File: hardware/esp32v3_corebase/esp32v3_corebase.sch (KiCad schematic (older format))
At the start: 47 parts, among them J1 USB_C_Receptacle_USB2.0, Q1 MBT2222ADW1T1, U1 TLV75533PDBV, U3 W25Q32FVSS, U4 CH340C, U5 ESP32, Y1 40MHz 10ppm

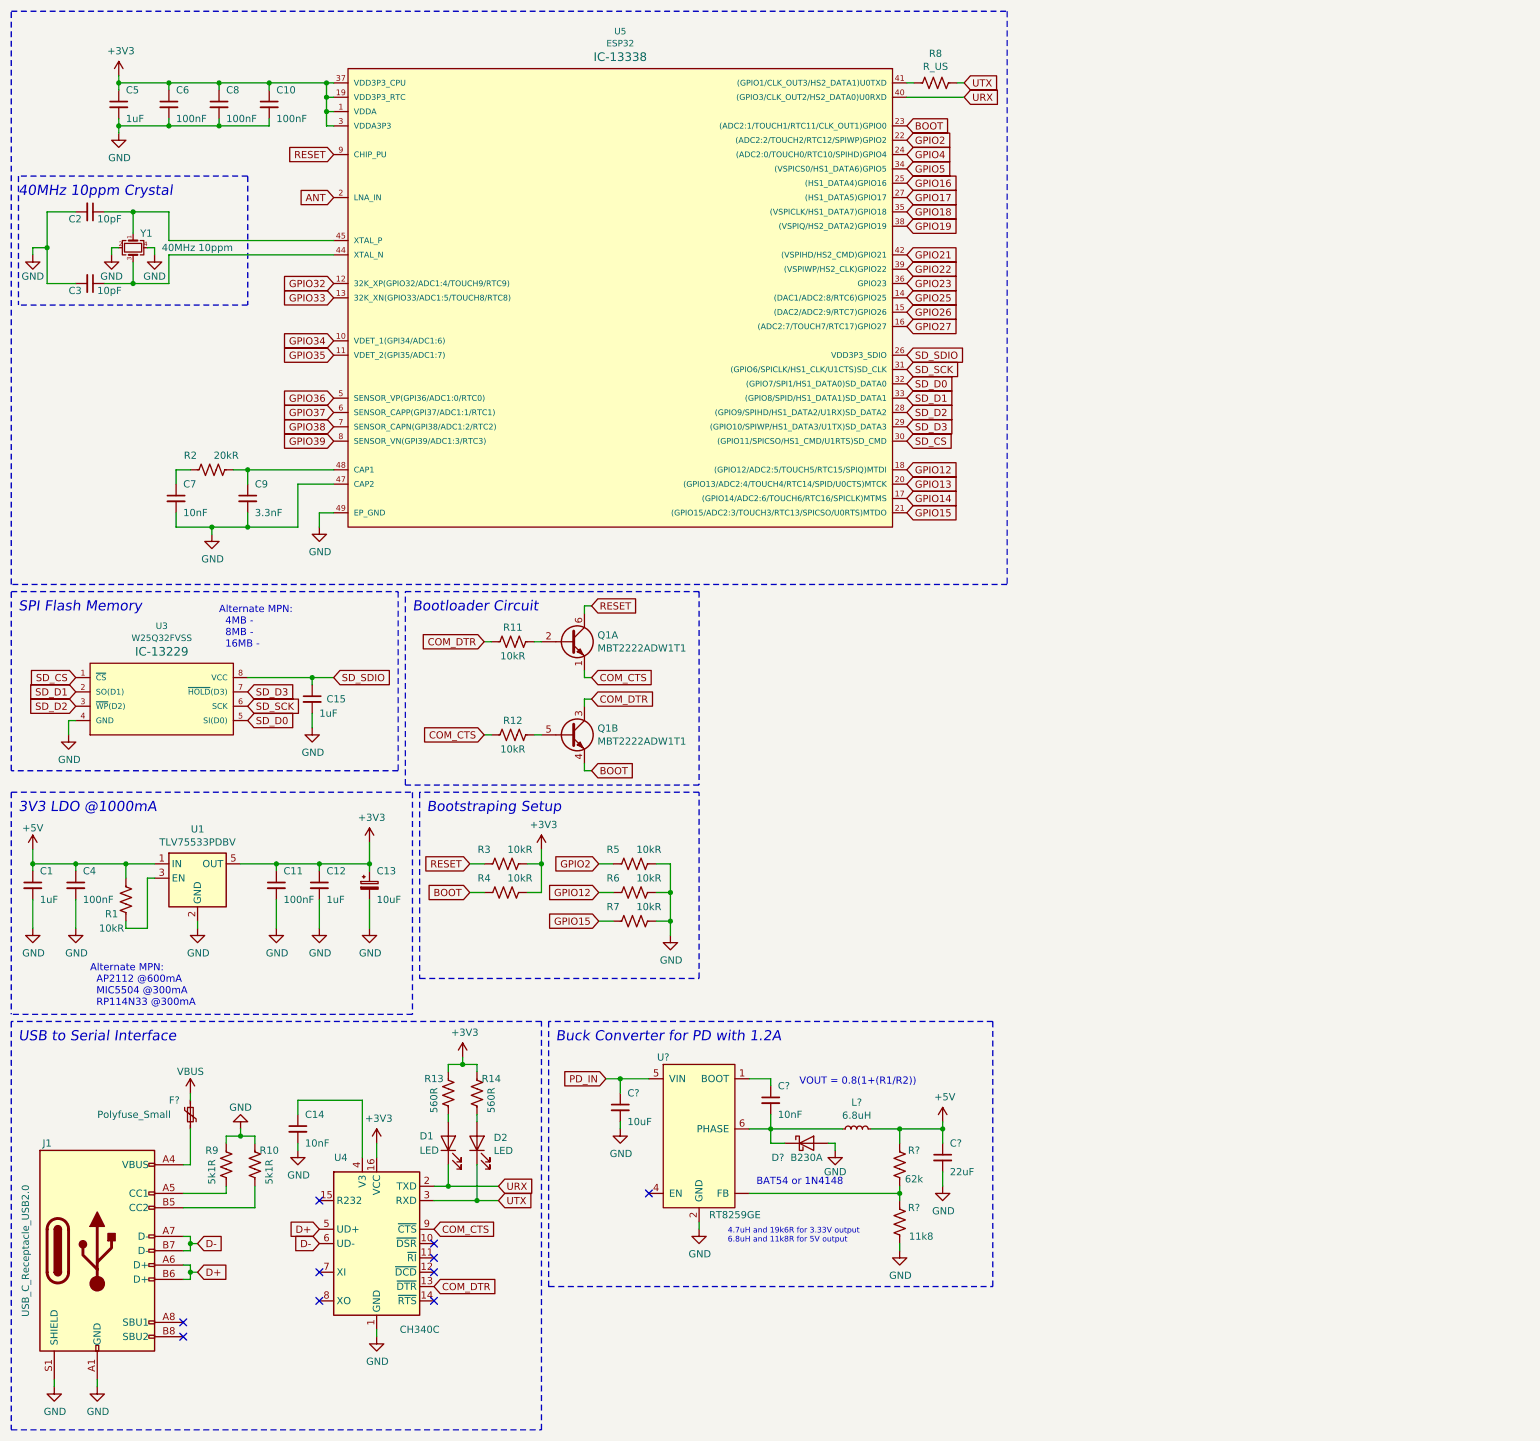
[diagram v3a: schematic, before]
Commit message: Added PSRAM and minor changes on sch
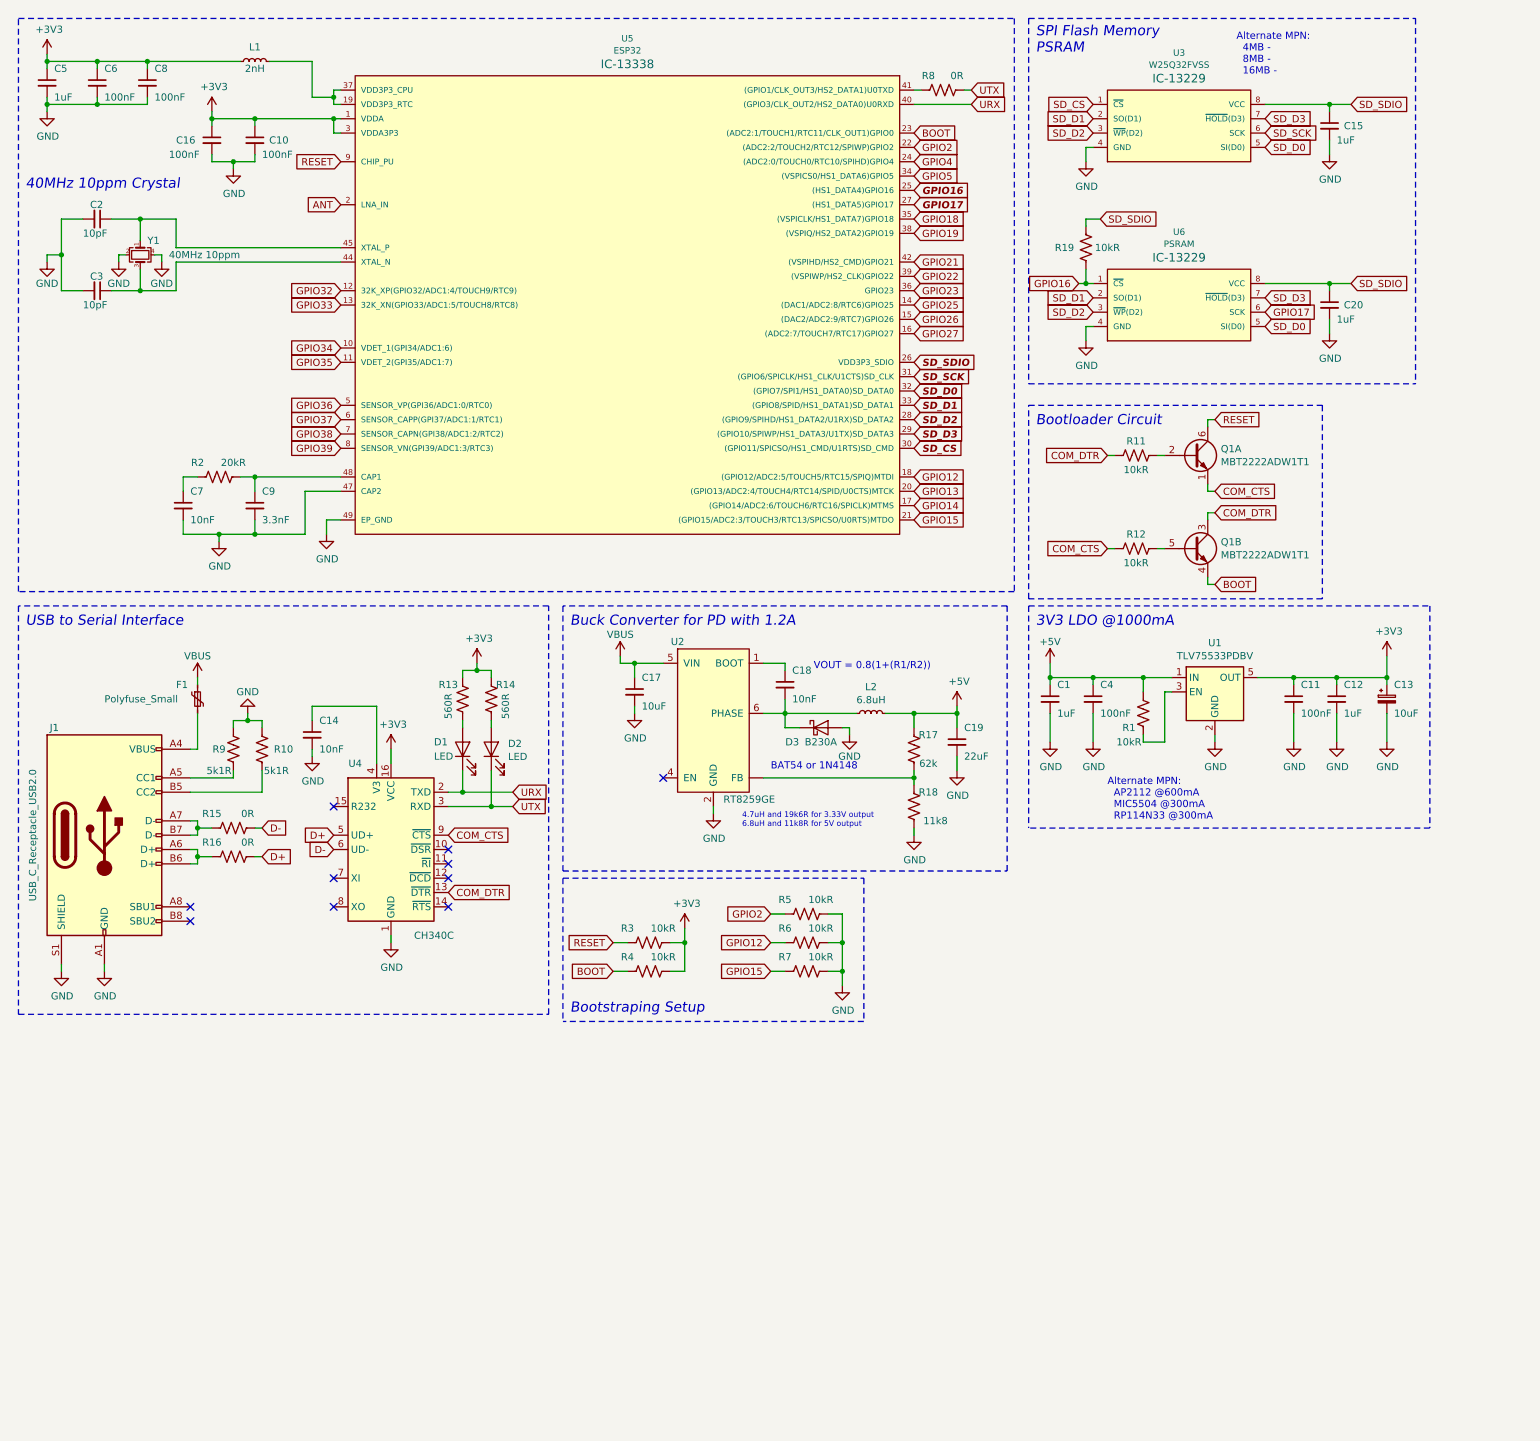
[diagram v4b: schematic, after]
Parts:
- added C16: 100nF, Capacitor_SMD:C_0402_1005Metric, symbol Device:C_Small
- added C20: 1uF, Capacitor_SMD:C_0603_1608Metric, symbol Device:C_Small
- added L1: 2nH, symbol Device:L_Small
- added R15, R16: 0R, Resistor_SMD:R_0402_1005Metric, symbol Device:R_US
- added R19: 10kR, Resistor_SMD:R_0402_1005Metric, symbol Device:R_US
- added U6: PSRAM, Silicon-Standard:SOIC-8, symbol SparkFun-IC-Memory:W25Q32FVSS
- R8: value R_US -> 0R
- gave numbers to parts that had none: 9
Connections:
- net PD_IN is gone; now on net VBUS: C17.1, U2.5 (VIN)
- net +3V3: now also C16.1, L1.1; no longer U5.19 (VDD3P3_RTC), U5.37 (VDD3P3_CPU)
- net D+: now also R16.1; no longer J1.A6 (D+), J1.B6 (D+)
- net D-: now also R15.1; no longer J1.A7 (D-), J1.B7 (D-)
- net GND: now also C16.2, C20.2, U6.4 (GND)
- net GPIO16: now also R19.1, U6.1 (~CS~)
- net GPIO17: now also U6.6 (SCK)
- net SD_D0: now also U6.5 (SI(D0))
- net SD_D1: now also U6.2 (SO(D1))
- net SD_D2: now also U6.3 (~WP~(D2))
- net SD_D3: now also U6.7 (~HOLD~(D3))
- net SD_SDIO: now also C20.1, R19.2, U6.8 (VCC)
- new net: J1.A6 (D+), J1.B6 (D+), R16.2
- new net: J1.A7 (D-), J1.B7 (D-), R15.2
- new net: L1.2, U5.19 (VDD3P3_RTC), U5.37 (VDD3P3_CPU)
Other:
- note added: "SPI Flash Memory\nPSRAM"
- note removed: "SPI Flash Memory"
- moved on the sheet: C1, C10, C11, C12, C13, C14, C15, C17, C18, C19, C2, C3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

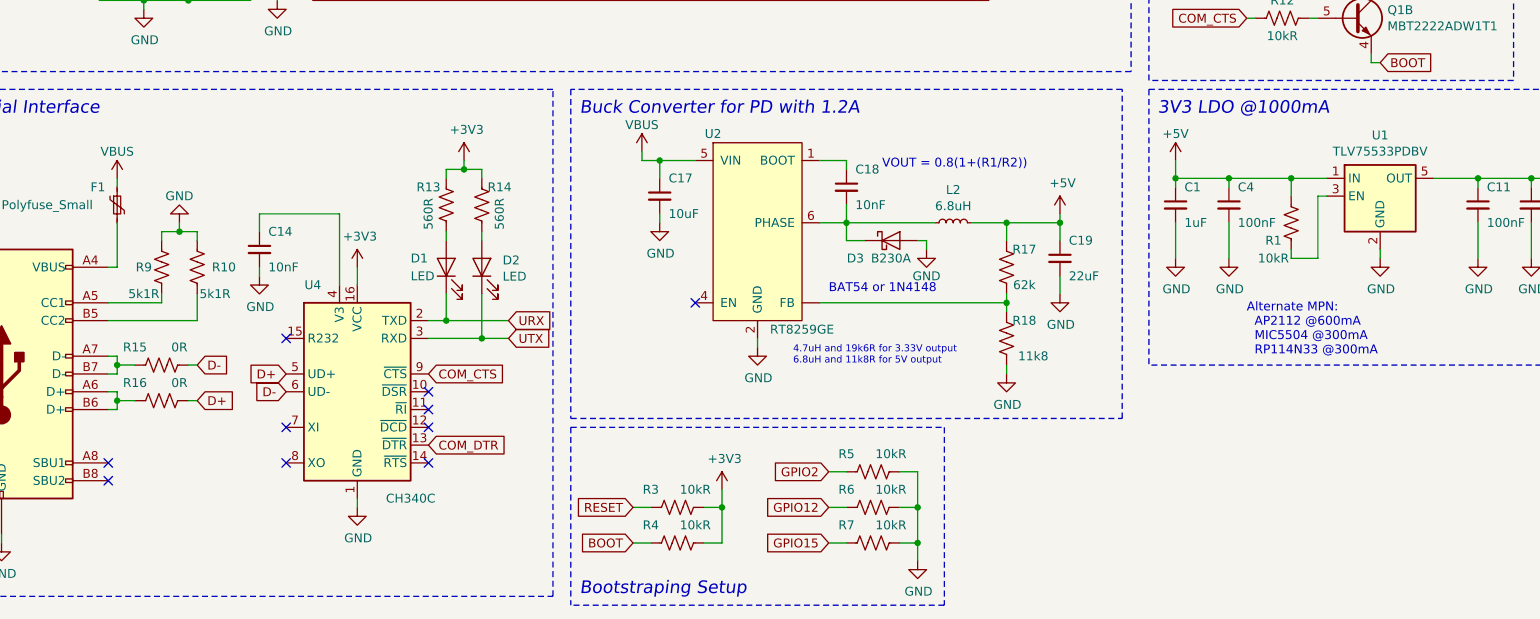
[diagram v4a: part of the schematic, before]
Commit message: Added 12MHz crystal for the CH340G version
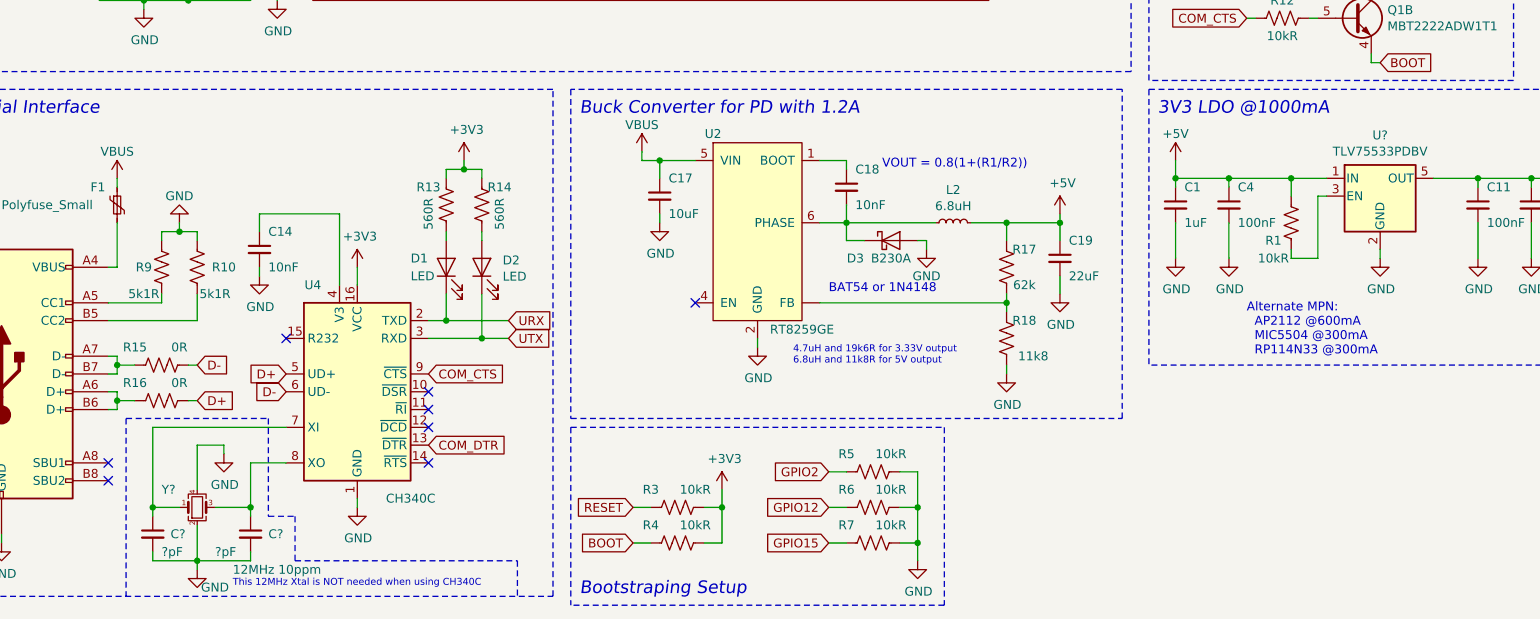
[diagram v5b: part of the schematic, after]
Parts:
- removed U1: TLV75533PDBV, Package_TO_SOT_SMD:SOT-23-5, symbol esp32v3_corebase-rescue:TLV75533PDBV-Regulator_Linear
- added C? (x2): ?pF, Capacitor_SMD:C_0402_1005Metric, symbol Device:C_Small
- added U?: TLV75533PDBV, Package_TO_SOT_SMD:SOT-23-5, symbol Regulator_Linear:TLV75533PDBV
- added Y?: 12MHz 10ppm, Clocks:CRYSTAL-SMD-3.2X2.5MM, symbol Device:Crystal_GND24_Small
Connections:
- net +3V3: now also U?.5 (OUT)
- net +5V: now also U?.1 (IN)
- net GND: now also C?.2, C?.2, U?.2 (GND), Y?.2, Y?.4
- net at R1.1: now also U?.3 (EN)
- net at U4.7 (XI): now also C?.1, Y?.1
- net at U4.8 (XO): now also C?.1, Y?.3
- no-connect marks 10 -> 8
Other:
- note added: "This 12MHz Xtal is NOT needed when using CH340C"
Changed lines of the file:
@@
 $EndDescr
-$Comp
-L esp32v3_corebase-rescue:TLV75533PDBV-Regulator_Linear U1
-U 1 1 5EB4877F
-P 8950 5250
-F 0 "U1" H 8950 5592 50  0000 C CNN
-F 1 "TLV75533PDBV" H 8950 5501 50  0000 C CNN
-F 2 "Package_TO_SOT_SMD:SOT-23-5" H 8950 5550 50  0001 C CIN
-F 3 "http://www.ti.com/lit/ds/symlink/tlv755p.pdf" H 8950 5250 50  0001 C CNN
-	1    8950 5250
-	1    0    0    -1
-$EndComp
 $Comp
 L power:GND #PWR0101
@@
 	1    0    0    -1
 $EndComp
-NoConn ~ 2800 6550
-NoConn ~ 2800 6750
 $Comp
 L Connector:USB_C_Receptacle_USB2.0 J1
@@
 Wire Wire Line
 	900  2450 1050 2450
+$Comp
+L Device:Crystal_GND24_Small Y?
+U 1 1 5F9F5EB0
+P 2300 7000
+F 0 "Y?" H 2100 7100 50  0000 L CNN
+F 1 "12MHz 10ppm" H 2500 6650 50  0000 L CNN
+F 2 "Clocks:CRYSTAL-SMD-3.2X2.5MM" H 2300 7000 50  0001 C CNN
+F 3 "~" H 2300 7000 50  0001 C CNN
+	1    2300 7000
+	1    0    0    -1
+$EndComp
+Wire Wire Line
+	2800 6550 2050 6550
+Wire Wire Line
+	2600 6750 2800 6750
+Wire Wire Line
+	2400 7000 2600 7000
+Wire Wire Line
+	2600 7000 2600 6750
+Wire Wire Line
+	2050 7000 2200 7000
+Wire Wire Line
+	2050 6550 2050 7000
+$Comp
+L power:GND #PWR?
+U 1 1 5FA2F4DE
+P 2450 6700
+F 0 "#PWR?" H 2450 6450 50  0001 C CNN
+F 1 "GND" H 2455 6527 50  0000 C CNN
+F 2 "" H 2450 6700 50  0001 C CNN
+F 3 "" H 2450 6700 50  0001 C CNN
+	1    2450 6700
+	1    0    0    -1
+$EndComp
+Wire Wire Line
+	2300 6900 2300 6650
+Wire Wire Line
+	2300 6650 2450 6650
+Wire Wire Line
+	2450 6650 2450 6700
+$Comp
+L power:GND #PWR?
+U 1 1 5FA3DBFF
+P 2300 7350
+F 0 "#PWR?" H 2300 7100 50  0001 C CNN
+F 1 "GND" H 2400 7250 50  0000 C CNN
+F 2 "" H 2300 7350 50  0001 C CNN
+F 3 "" H 2300 7350 50  0001 C CNN
+	1    2300 7350
+	1    0    0    -1
+$EndComp
+$Comp
+L Device:C_Small C?
+U 1 1 5FA4C70F
+P 2050 7150
+F 0 "C?" H 2150 7150 50  0000 L CNN
+F 1 "?pF" H 2100 7050 50  0000 L CNN
+F 2 "Capacitor_SMD:C_0402_1005Metric" H 2050 7150 50  0001 C CNN
+F 3 "~" H 2050 7150 50  0001 C CNN
+	1    2050 7150
+	1    0    0    -1
+$EndComp
+$Comp
+L Device:C_Small C?
+U 1 1 5FA9FCD0
+P 2600 7150
+F 0 "C?" H 2700 7150 50  0000 L CNN
+F 1 "?pF" H 2400 7050 50  0000 L CNN
+F 2 "Capacitor_SMD:C_0402_1005Metric" H 2600 7150 50  0001 C CNN
+F 3 "~" H 2600 7150 50  0001 C CNN
+	1    2600 7150
+	1    0    0    -1
+$EndComp
+Wire Wire Line
+	2050 7250 2050 7300
+Wire Wire Line
+	2050 7300 2300 7300
+Wire Wire Line
+	2300 7100 2300 7300
+Wire Wire Line
+	2300 7350 2300 7300
+Connection ~ 2300 7300
+Wire Wire Line
+	2600 7250 2600 7300
+Wire Wire Line
+	2600 7300 2300 7300
+Wire Wire Line
+	2600 7050 2600 7000
+Connection ~ 2600 7000
+Wire Wire Line
+	2050 7050 2050 7000
+Connection ~ 2050 7000
+Text Notes 2500 7450 0    39   ~ 0
+This 12MHz Xtal is NOT needed when using CH340C
+Wire Notes Line
+	2700 6500 2700 7050
+Wire Notes Line
+	2700 7050 2850 7050
+Wire Notes Line
+	2850 7050 2850 7300
+Wire Notes Line
+	2850 7300 4100 7300
+Wire Notes Line
+	4100 7300 4100 7500
+Wire Notes Line
+	1900 6500 1900 7500
+Wire Notes Line
+	1900 6500 2700 6500
+$Comp
+L Regulator_Linear:TLV75533PDBV U?
+U 1 1 5FB0C8EF
+P 8950 5250
+F 0 "U?" H 8950 5592 50  0000 C CNN
+F 1 "TLV75533PDBV" H 8950 5501 50  0000 C CNN
+F 2 "Package_TO_SOT_SMD:SOT-23-5" H 8950 5575 50  0001 C CIN
+F 3 "http://www.ti.com/lit/ds/symlink/tlv755p.pdf" H 8950 5300 50  0001 C CNN
+	1    8950 5250
+	1    0    0    -1
+$EndComp
 $EndSCHEMATC
